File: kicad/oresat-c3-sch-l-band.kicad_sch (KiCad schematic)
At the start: 71 parts, among them U15 Qorvo 856930, U16 AX5043, U17 SI4112, U2 BP0805A1308, U29 TQP3M9036, U3 BP0805A1308, U4 BGB741L7ESD, U5 BP0805A1308, U7 MAC-24+

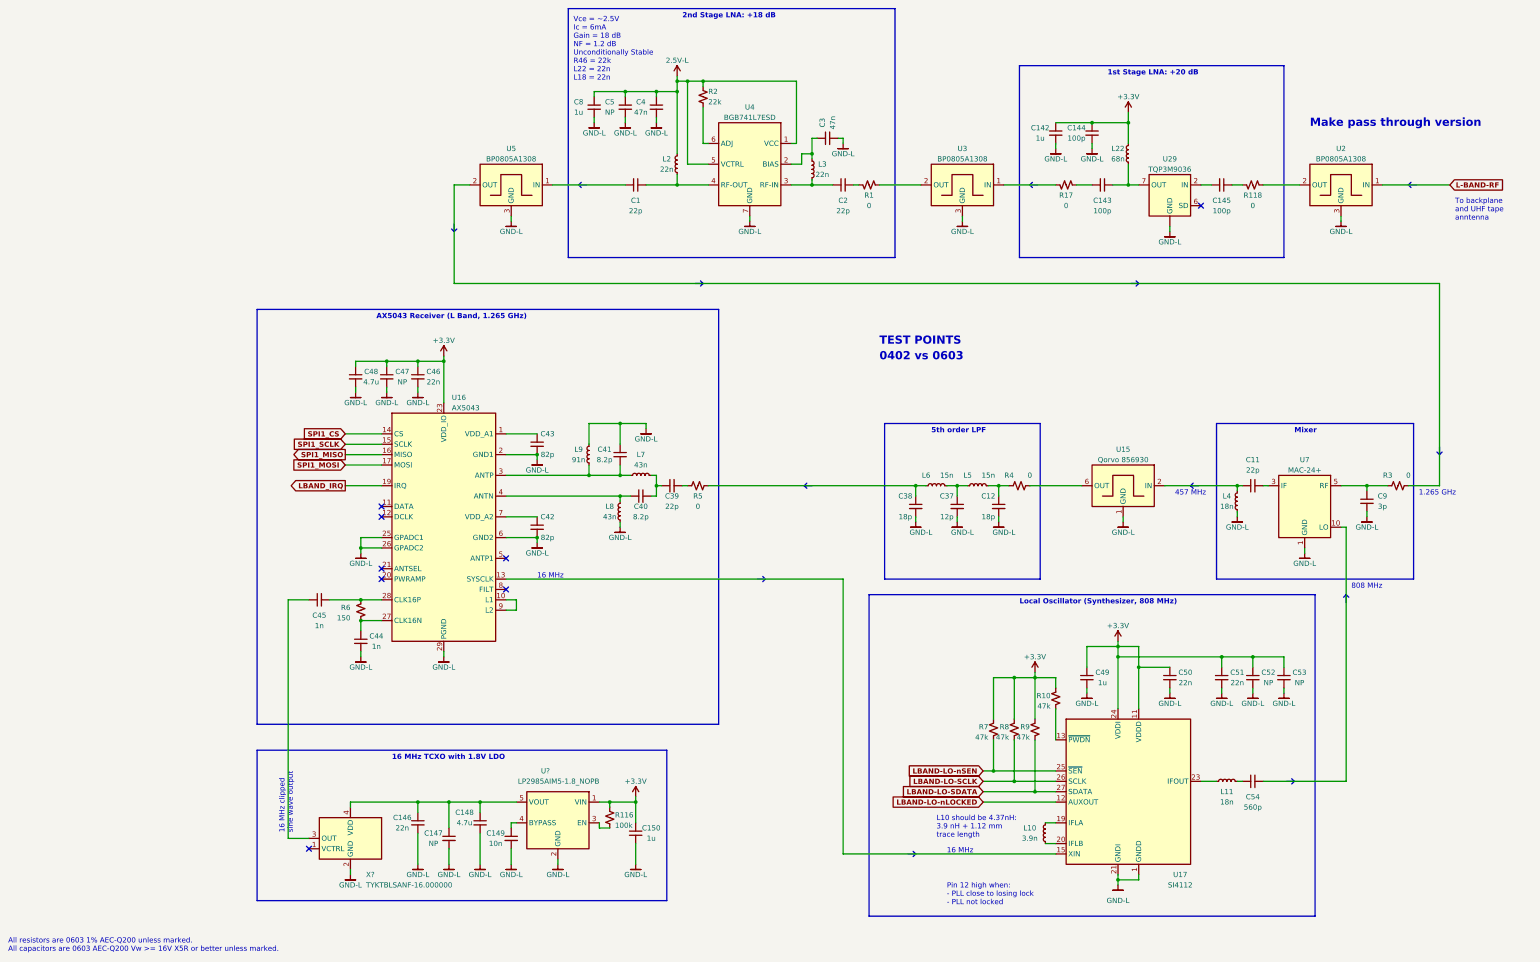
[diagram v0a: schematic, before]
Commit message: Big C3 cleanup with Glenn; radios off of one SPS + separate LDOs, removed lots of test 0 ohm resistors, cleaned up capacitance, and finally wired everything up to the octavo. ZERO ERC errors.
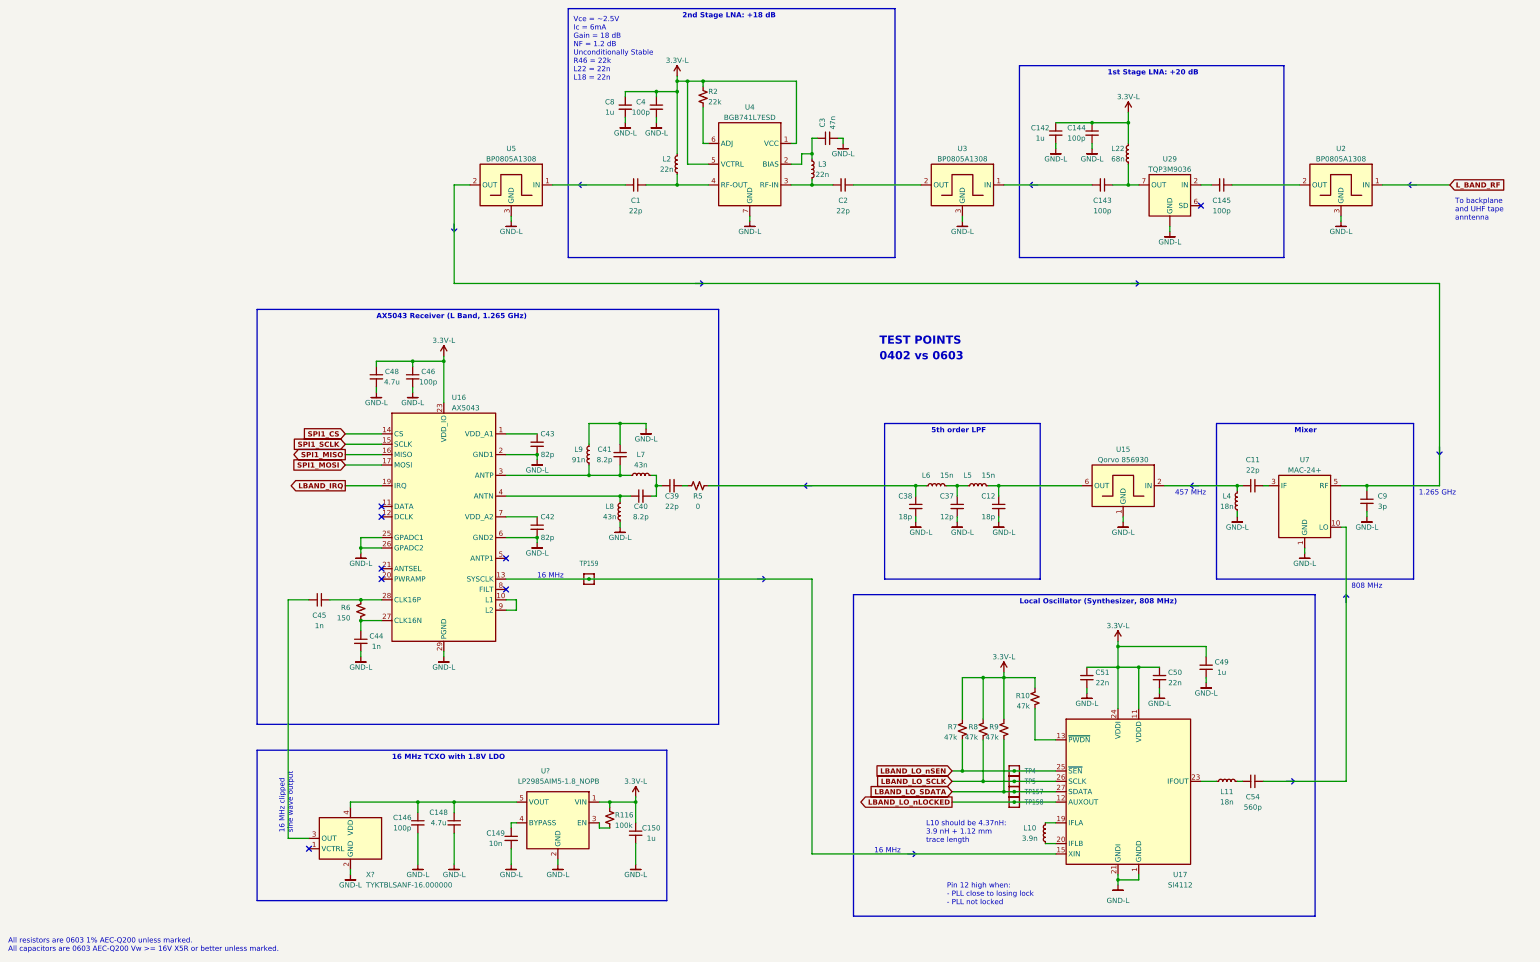
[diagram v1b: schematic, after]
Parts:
- removed C147, C47, C5, C52, C53: NP, Capacitor_SMD:C_0603_1608Metric, symbol Device:C_Small
- removed R1, R118, R17, R3, R4: 0, Resistor_SMD:R_0402_1005Metric, symbol Device:R_Small_US
- added TP157, TP158, TP159, TP4, TP5: Test-Point, TestPoint:TestPoint_Pad_D1.0mm, symbol oresat-misc:Test-Point-1mm-round
- C146, C46: value 22n -> 100p
- C4: value 47n -> 100p
- U?: footprint (none) -> Package_TO_SOT_SMD:SOT-23-5
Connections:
- net 3.3VA is gone; now on net 3.3V: C4.1, C8.1, L2.1, R2.1, U4.1 (VCC), U4.5 (VCTRL)
- net at U2.2 (OUT): now also C145.1
- net at U16.13 (SYSCLK), U17.15 (XIN): now also TP159.1
- net at C12.1, L5.2: now also U15.6 (OUT)
- net at C9.1, U7.5 (RF): now also U5.2 (OUT)
- net at U3.1 (IN): now also C143.2
- net at U3.2 (OUT): now also C2.1
- net +3.3V renamed 3.3V
- net L-BAND-RF renamed L_BAND_RF
- net LBAND-LO-SCLK renamed LBAND_LO_SCLK
- net LBAND_LO_SCLK: now also TP5.1
- net LBAND-LO-SDATA renamed LBAND_LO_SDATA
- net LBAND_LO_SDATA: now also TP157.1
- net LBAND-LO-nLOCKED renamed LBAND_LO_nLOCKED
- net LBAND_LO_nLOCKED: now also TP158.1
- net LBAND-LO-nSEN renamed LBAND_LO_nSEN
- net LBAND_LO_nSEN: now also TP4.1
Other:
- note removed: "Make pass through version"
- moved on the sheet: C148, C46, C48, C49, C50, C51, C8, R10, R7, R8, R9

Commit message: Updated test points, fixed some more hidden ERCs.
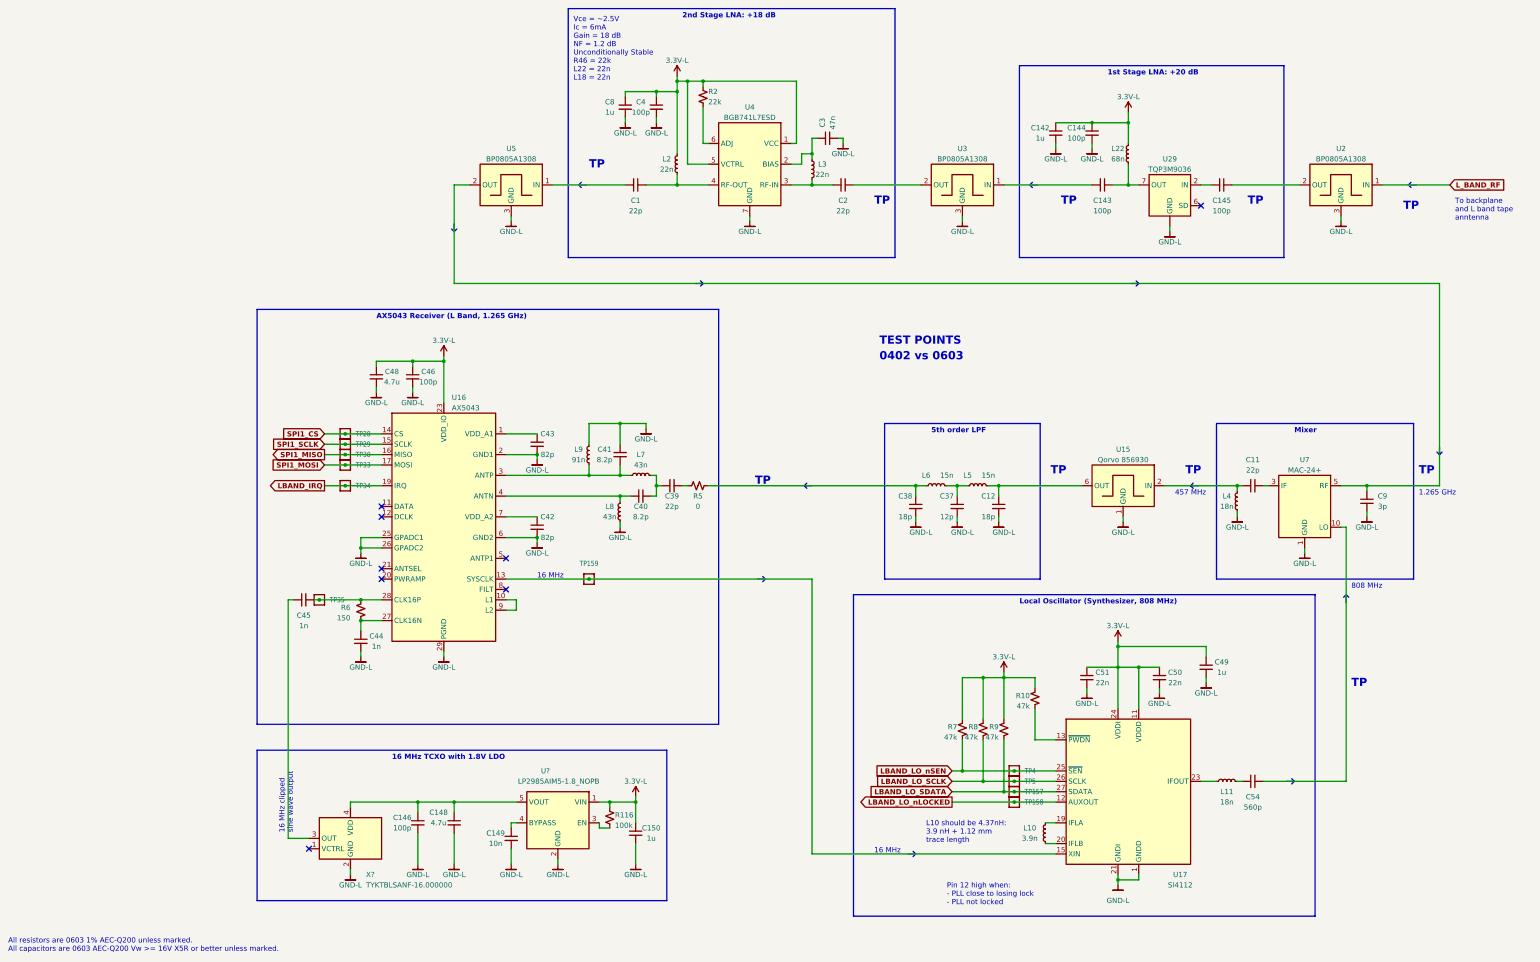
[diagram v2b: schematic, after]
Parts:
- added TP28, TP29, TP30, TP33, TP34, TP35: Test-Point, TestPoint:TestPoint_Pad_D1.0mm, symbol oresat-misc:Test-Point-1mm-round
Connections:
- net LBAND_IRQ: now also TP34.1
- net SPI1_CS: now also TP28.1
- net SPI1_MISO: now also TP30.1
- net SPI1_MOSI: now also TP33.1
- net SPI1_SCLK: now also TP29.1
- net at C45.2, R6.1, U16.28 (CLK16P): now also TP35.1
- net 3.3V renamed 3.3V-L
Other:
- note added: "TP"
- note added: "To backplane and L band tape anntenna"
- note removed: "To backplane and UHF tape anntenna"
- moved on the sheet: C45

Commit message: Fixed test points; added RF test points. Started on layout and component packages for UHF radio.
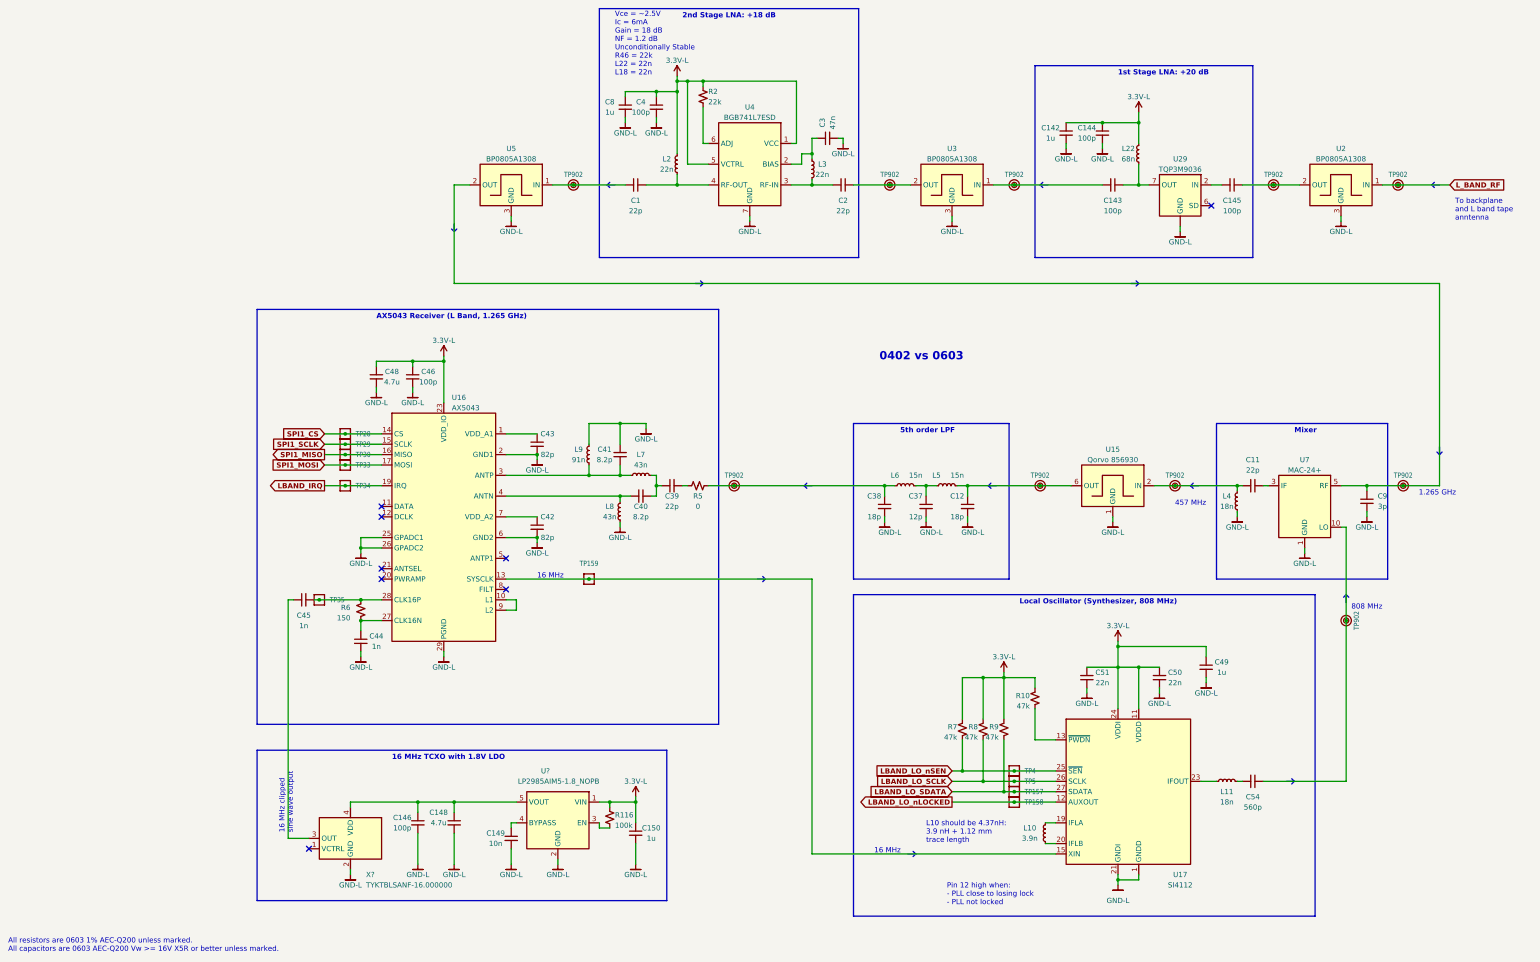
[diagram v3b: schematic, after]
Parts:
- added TP902 (x10): ~, oresat-misc:TestPoint_RF_Probe, symbol oresat-misc:Test-Point-RF-Probe-Stripline
- TP157, TP158, TP159, TP28, TP29, TP30, TP33, TP34, TP35, TP4, TP5: footprint TestPoint:TestPoint_Pad_D1.0mm -> oresat-misc:TestPoint_Pad_D1.0mm
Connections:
- net L_BAND_RF: now also TP902.1
- net at C145.1, U2.2 (OUT): now also TP902.1
- net at C38.1, L6.1, R5.2: now also TP902.1
- net at C11.1, L4.1, U15.2 (IN): now also TP902.1
- net at C12.1, L5.2, U15.6 (OUT): now also TP902.1
- net at C143.2, U3.1 (IN): now also TP902.1
- net at C2.1, U3.2 (OUT): now also TP902.1
- net at C1.2, U5.1 (IN): now also TP902.1
- net at C9.1, U5.2 (OUT), U7.5 (RF): now also TP902.1
- net at C54.2, U7.10 (LO): now also TP902.1
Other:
- note removed: "TEST POINTS"
- note removed: "TP"
- moved on the sheet: C12, C142, C143, C144, C145, C37, C38, L22, L5, L6, U15, U29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

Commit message: More progress on the UHF band radio.
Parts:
- U29: footprint (none) -> oresat-ics:U-Qorvo-TQP3M9036-QFN-8-MO-220E
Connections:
- net GND: now also U29.EP (GND); no longer U29. (GND)
- new net: U29.1, U29.3, U29.4, U29.8
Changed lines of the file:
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@@
       (effects (font (size 1.27 1.27)))
     )
-    (property "Footprint" "" (at 308.61 52.07 0)
+    (property "Footprint" "oresat-ics:U-Qorvo-TQP3M9036-QFN-8-MO-220E" (at 308.61 52.07 0)
       (effects (font (size 1.27 1.27)) hide)
     )
-    (property "Datasheet" "https://www.mouser.com/datasheet/2/412/TQP3M9036_Data_Sheet-1500677.pdf" (at 308.61 52.07 0)
+    (property "Datasheet" "https://www.qorvo.com/products/d/da005543" (at 308.61 52.07 0)
       (effects (font (size 1.27 1.27)) hide)
     )
-    (pin "")
+    (pin "1")
     (pin "2")
+    (pin "3")
+    (pin "4")
     (pin "6")
     (pin "7")
+    (pin "8")
+    (pin "EP")
     (instances
       (project "oresat-c3"

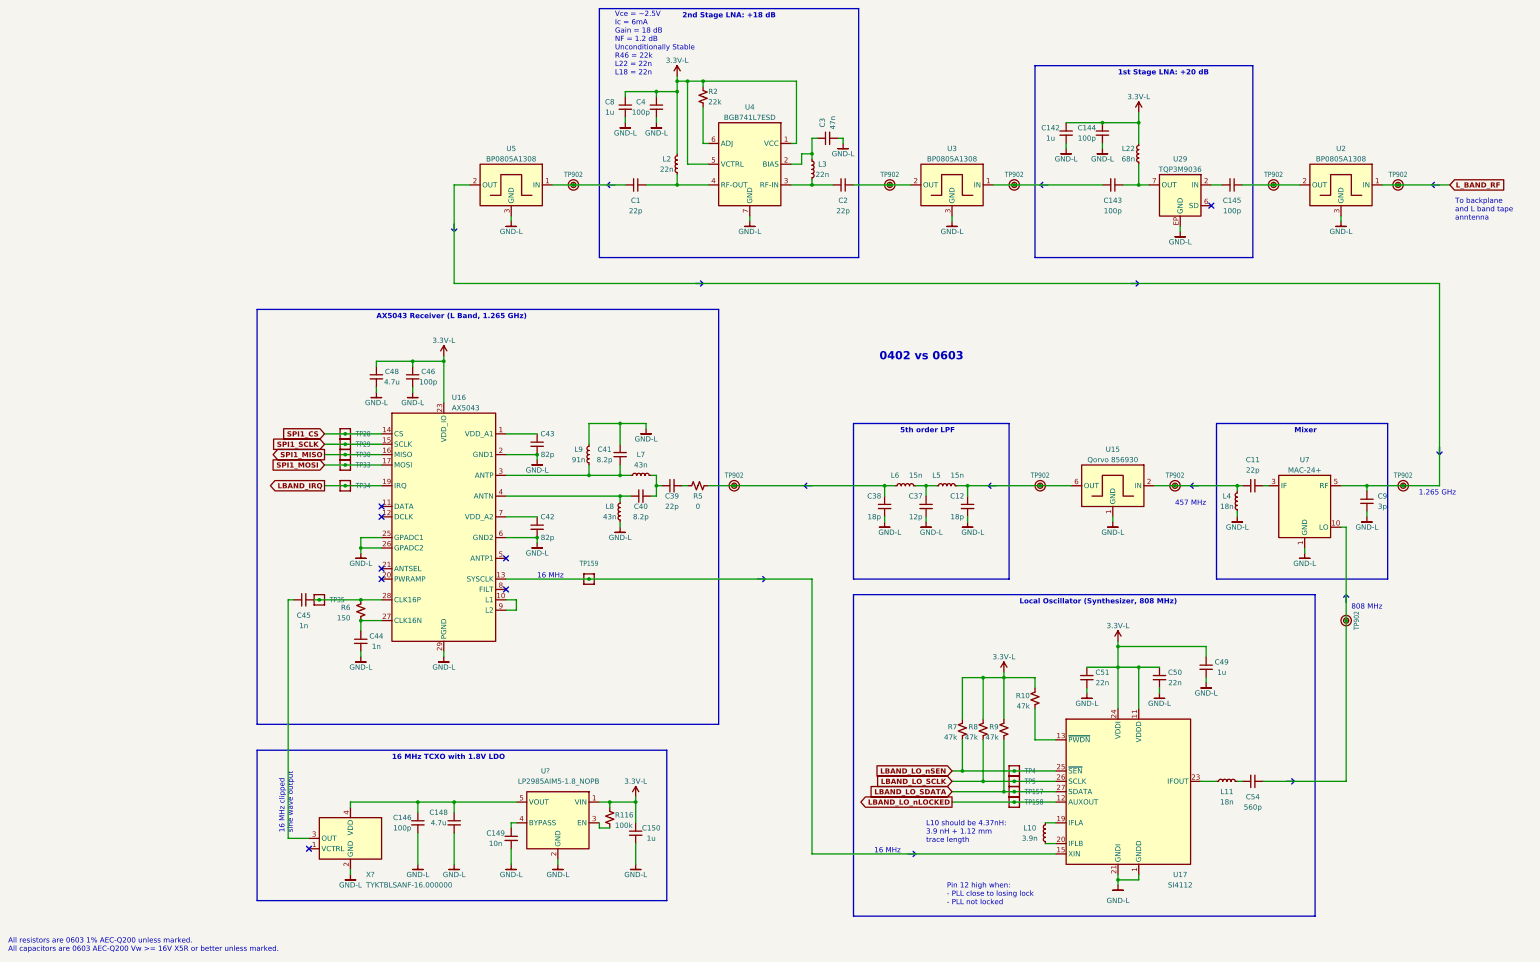
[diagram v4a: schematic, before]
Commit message: Fixed footprints and laid out WDT and OPD circuitry.
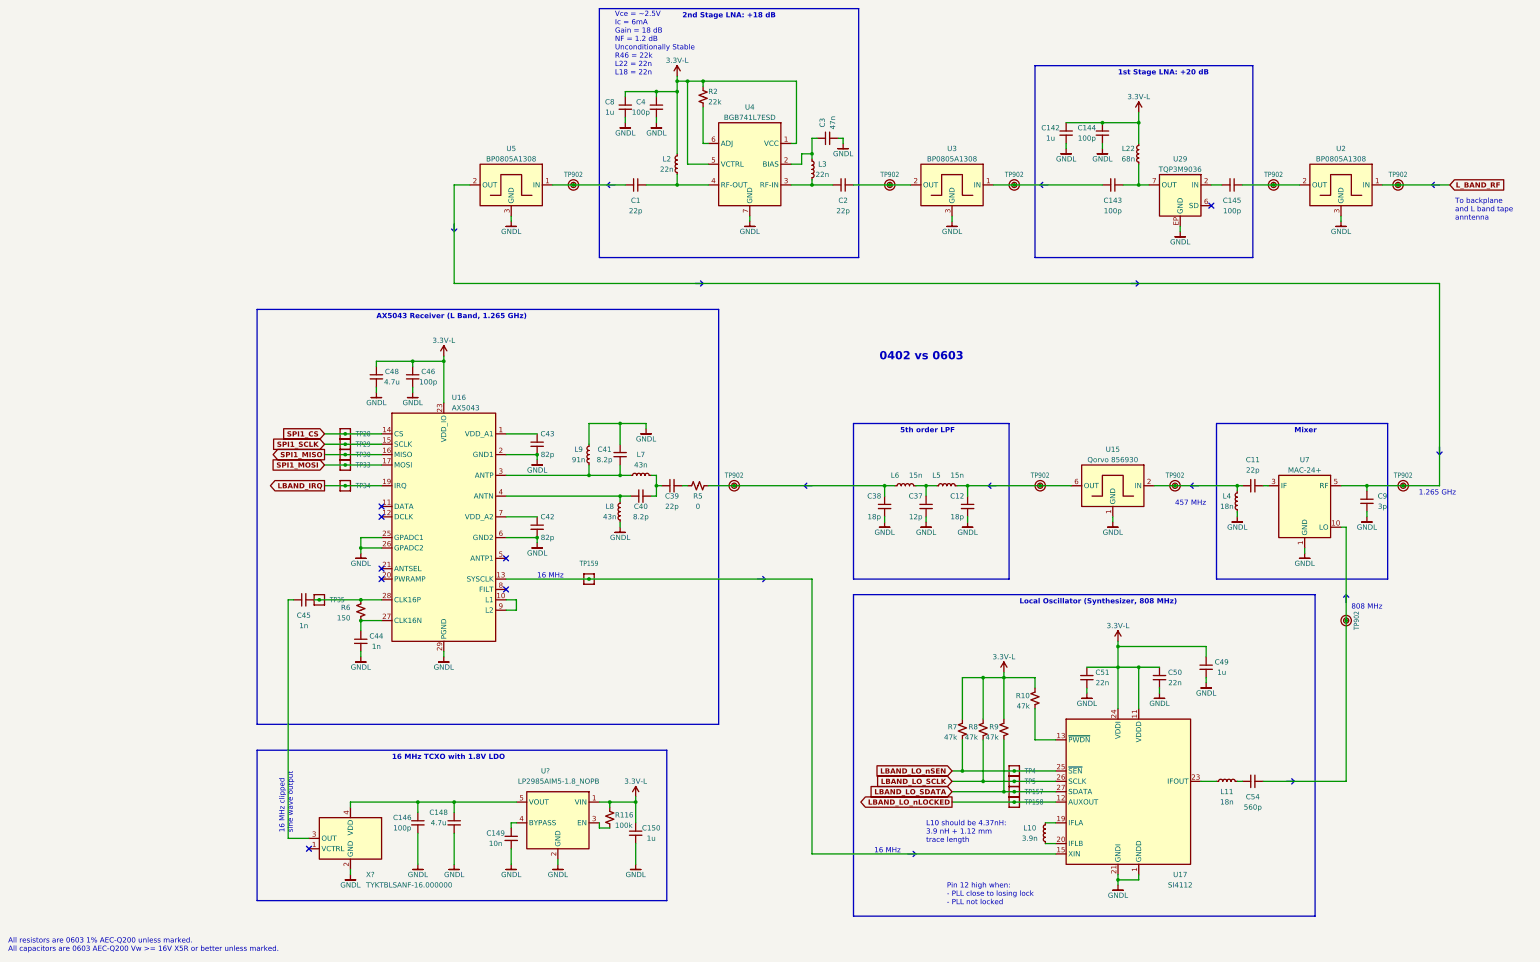
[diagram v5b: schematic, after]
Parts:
- X?: footprint (none) -> oresat-ics:X_TCXO_SMD_Taitien_2.5x2.0mm; symbol oresat-ics:TAITIEN-TY -> oresat-ics:Taiten-TY-Series-TXCO
